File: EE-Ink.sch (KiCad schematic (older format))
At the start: 3 parts

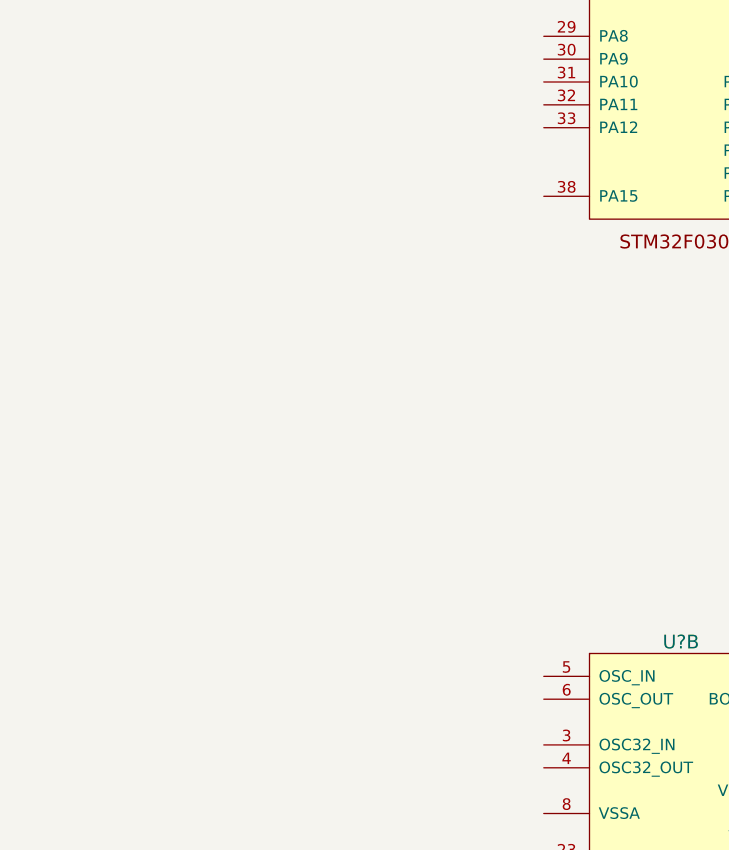
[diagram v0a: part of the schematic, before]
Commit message: Created drawing for the E-ink display and plopped it onto the schematic.
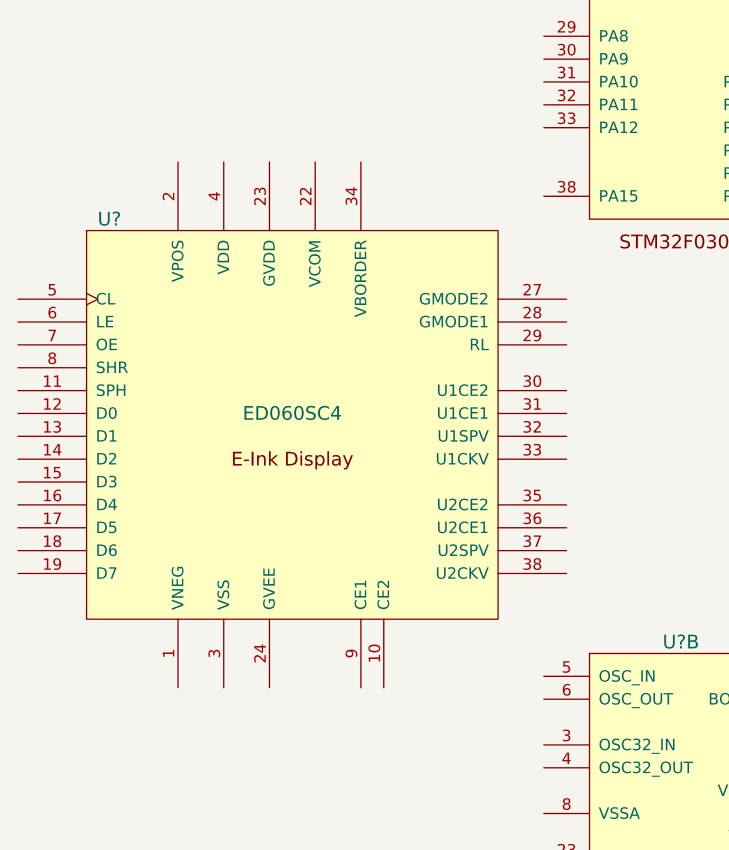
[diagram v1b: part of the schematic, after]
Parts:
- added U?: ED060SC4, symbol ED060SC4
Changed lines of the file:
@@
 LIBS:valves
 LIBS:stm32
+LIBS:e-ink
+LIBS:EE-Ink-cache
 EELAYER 25 0
 EELAYER END
@@
 	1    0    0    -1
 $EndComp
+$Comp
+L ED060SC4 U?
+U 1 1 58D7DC1F
+P 2250 4250
+F 0 "U?" H 1450 5150 60  0000 C CNN
+F 1 "ED060SC4" H 2250 4300 60  0000 C CNN
+F 2 "" H 2250 4250 60  0000 C CNN
+F 3 "" H 2250 4250 60  0000 C CNN
+	1    2250 4250
+	1    0    0    -1
+$EndComp

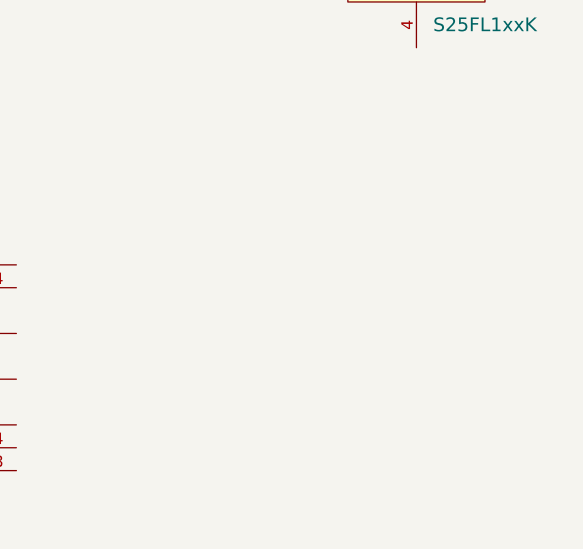
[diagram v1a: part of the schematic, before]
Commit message: Added dc to dc converter component.
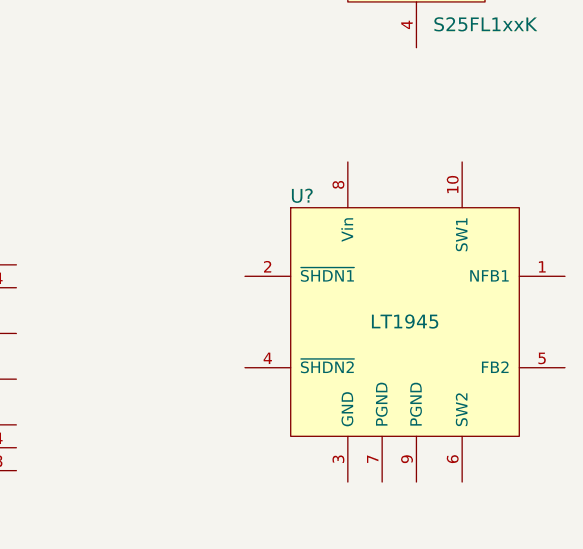
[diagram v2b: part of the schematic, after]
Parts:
- added U?: LT1945, symbol LT1945
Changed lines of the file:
@@
+	1    0    0    -1
+$EndComp
+$Comp
+L LT1945 U?
+U 1 1 58D7E9C0
+P 6250 5600
+F 0 "U?" H 5800 6150 60  0000 C CNN
+F 1 "LT1945" H 6250 5600 60  0000 C CNN
+F 2 "" H 6250 5600 60  0001 C CNN
+F 3 "" H 6250 5600 60  0001 C CNN
+	1    6250 5600
 	1    0    0    -1
 $EndComp

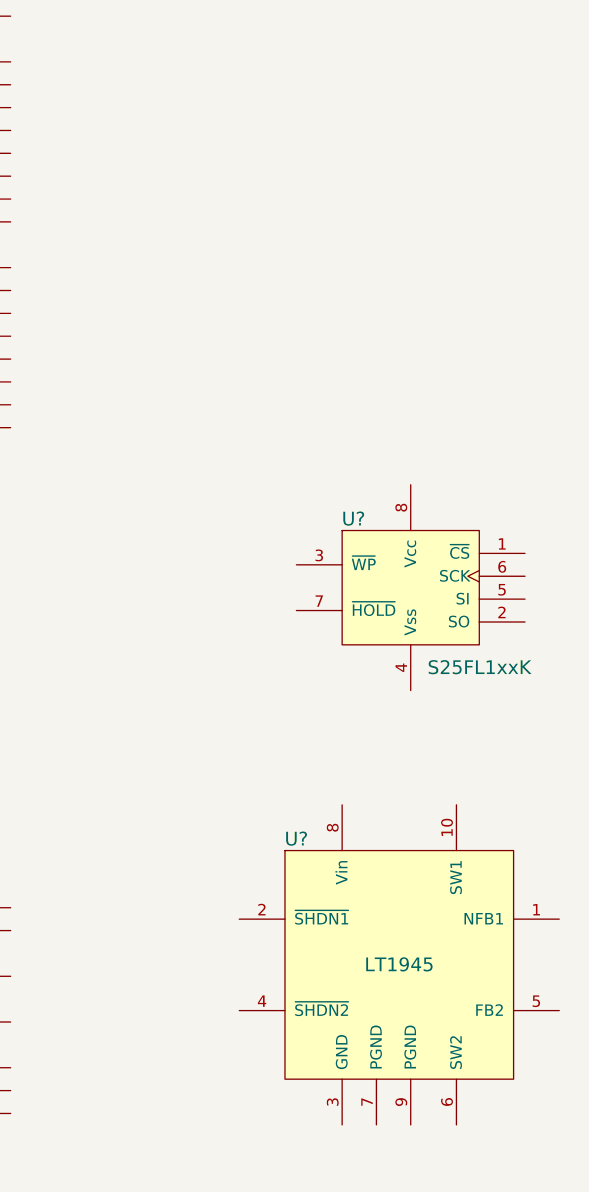
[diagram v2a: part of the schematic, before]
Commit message: Added battery charger component.
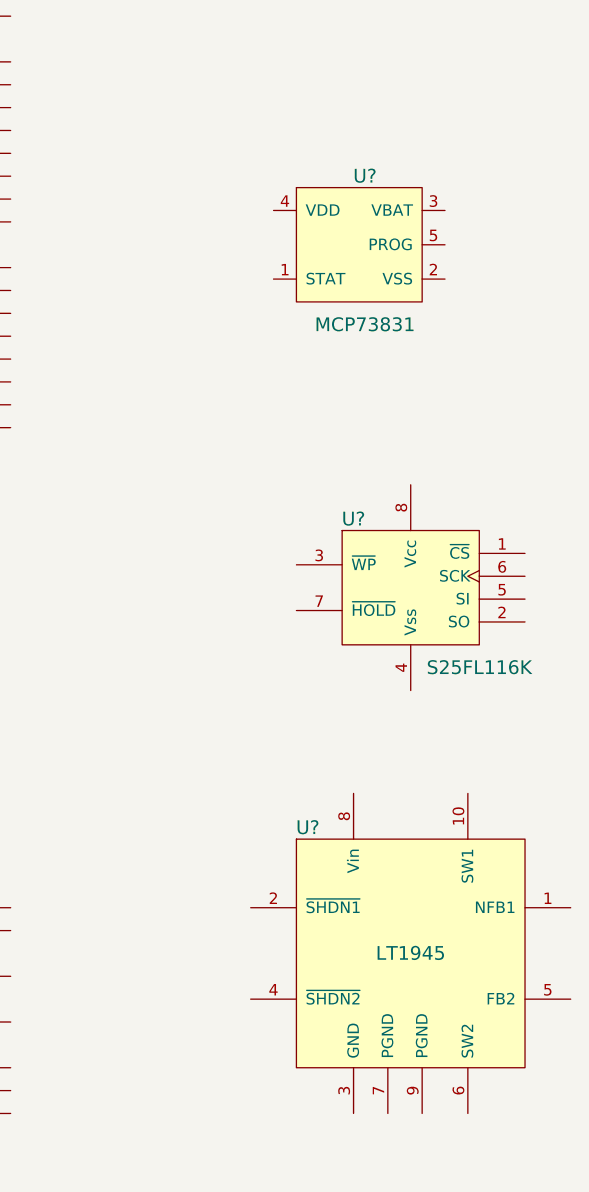
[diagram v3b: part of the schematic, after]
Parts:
- added U?: MCP73831, TO_SOT_Packages_SMD:SOT-23-5, symbol MCP73831
- U?: value S25FL1xxK -> S25FL116K
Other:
- moved on the sheet: U?
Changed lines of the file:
@@
 LIBS:stm32
 LIBS:e-ink
+LIBS:battery
 LIBS:EE-Ink-cache
 EELAYER 25 0
@@
 P 6300 3950
 F 0 "U?" H 6050 4250 60  0000 C CNN
-F 1 "S25FL1xxK" H 6600 3600 60  0000 C CNN
+F 1 "S25FL116K" H 6600 3600 60  0000 C CNN
 F 2 "" H 6200 4000 60  0001 C CNN
 F 3 "" H 6200 4000 60  0001 C CNN
@@
 L LT1945 U?
 U 1 1 58D7E9C0
-P 6250 5600
-F 0 "U?" H 5800 6150 60  0000 C CNN
-F 1 "LT1945" H 6250 5600 60  0000 C CNN
-F 2 "" H 6250 5600 60  0001 C CNN
-F 3 "" H 6250 5600 60  0001 C CNN
-	1    6250 5600
+P 6300 5550
+F 0 "U?" H 5850 6100 60  0000 C CNN
+F 1 "LT1945" H 6300 5550 60  0000 C CNN
+F 2 "" H 6300 5550 60  0001 C CNN
+F 3 "" H 6300 5550 60  0001 C CNN
+	1    6300 5550
 	1    0    0    -1
 $EndComp
+$Comp
+L MCP73831 U?
+U 1 1 58D81AF5
+P 6100 2450
+F 0 "U?" H 6100 2750 60  0000 C CNN
+F 1 "MCP73831" H 6100 2100 60  0000 C CNN
+F 2 "TO_SOT_Packages_SMD:SOT-23-5" H 6100 1900 60  0001 C CNN
+F 3 "https://www.adafruit.com/datasheets/MCP73831.pdf" H 6100 2000 60  0001 C CNN
+	1    6100 2450
+	1    0    0    -1
+$EndComp

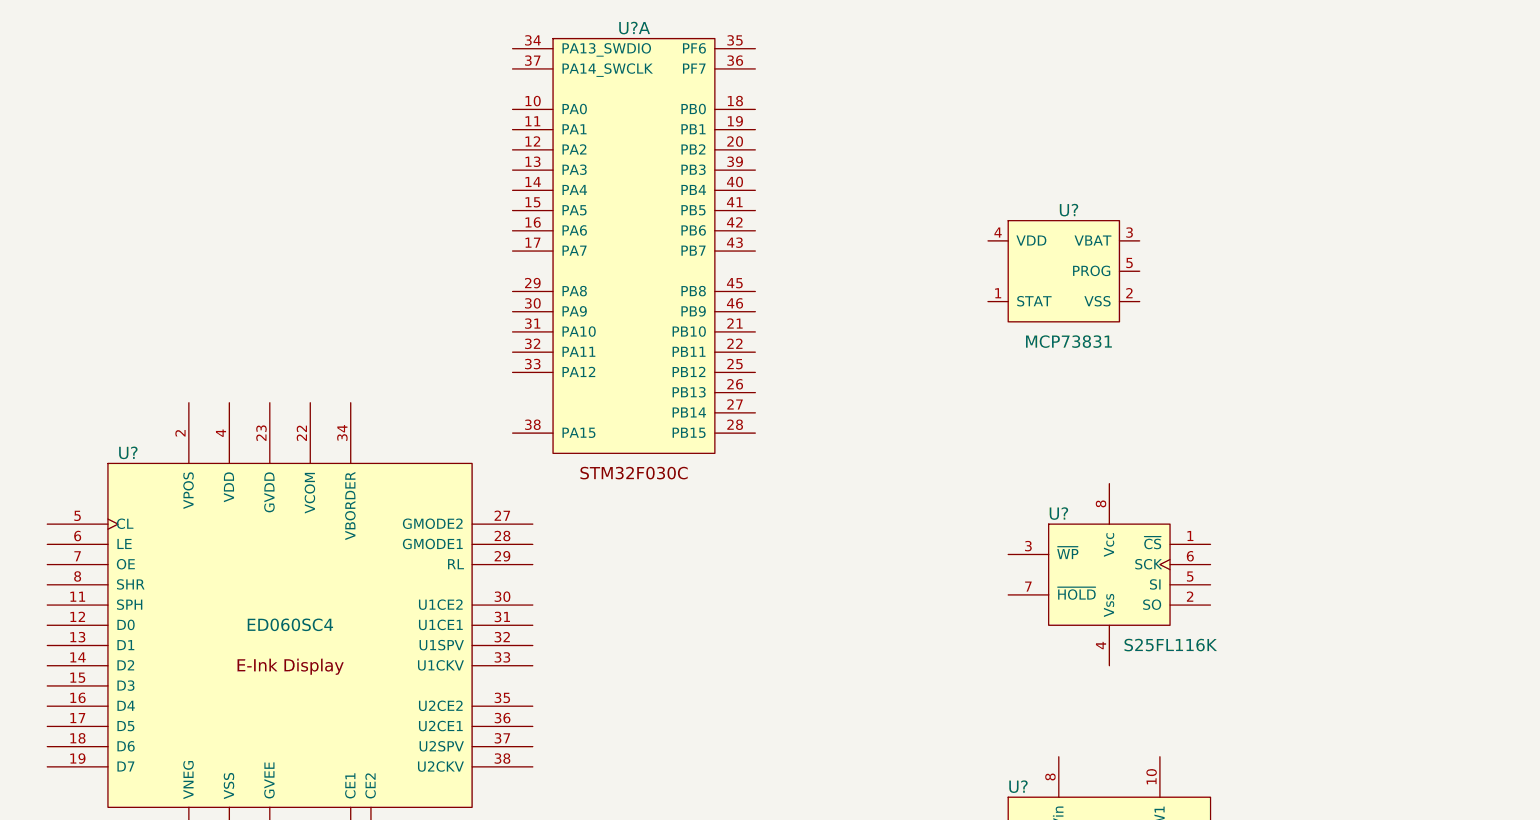
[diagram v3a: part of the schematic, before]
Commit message: Added several components.
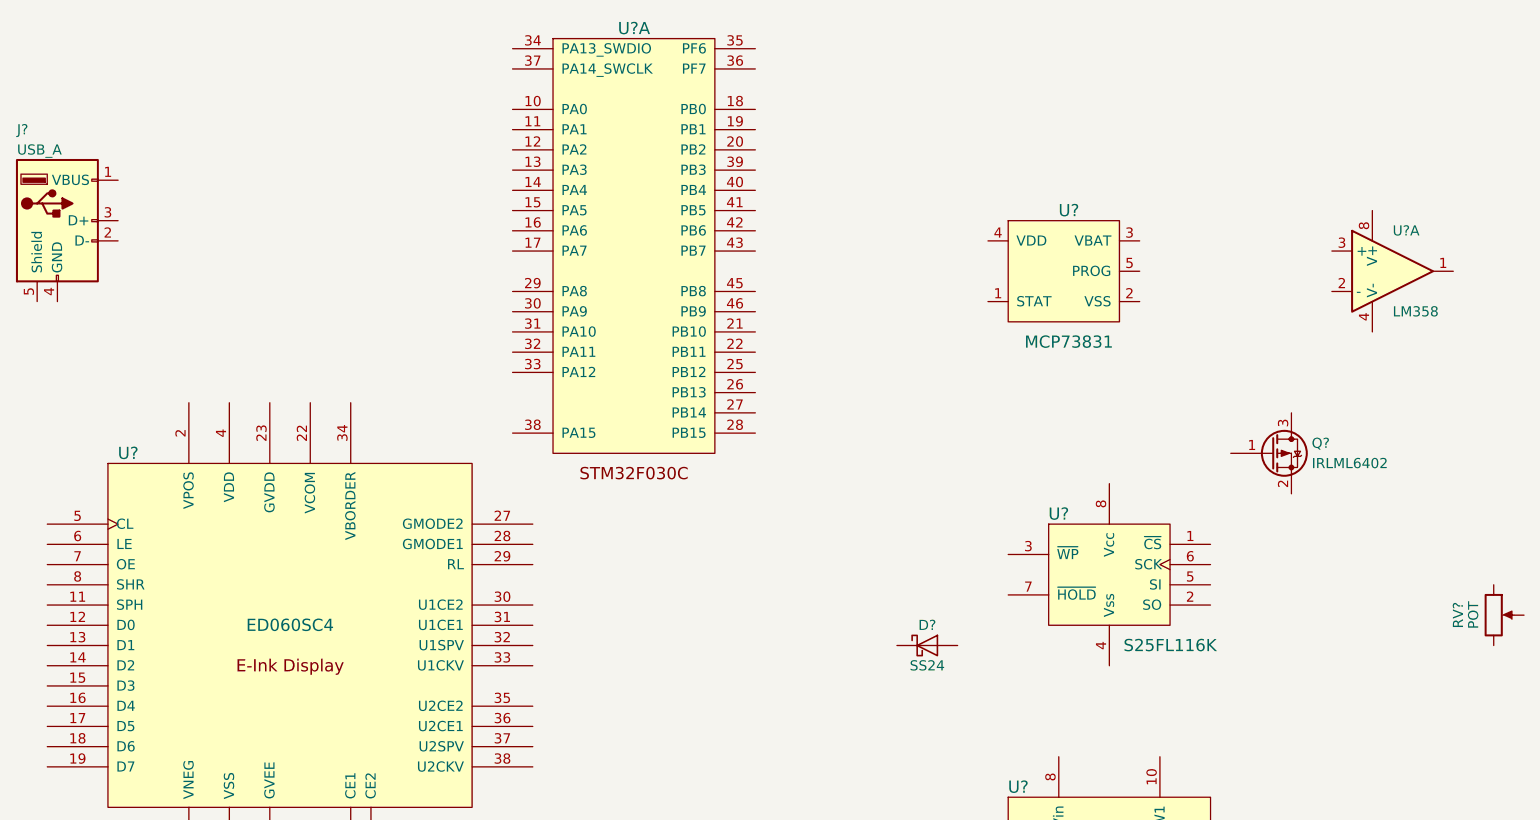
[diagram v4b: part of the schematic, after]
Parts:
- added D?: SS24, symbol D_Schottky
- added J?: USB_A, symbol USB_A
- added Q?: IRLML6402, symbol Q_PMOS_GSD
- added RV?: POT, symbol POT
- added U?: LM358, symbol LM358
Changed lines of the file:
@@
+	1    0    0    -1
+$EndComp
+$Comp
+L LM358 U?
+U 1 1 58D822C9
+P 7700 2450
+F 0 "U?" H 7700 2650 50  0000 L CNN
+F 1 "LM358" H 7700 2250 50  0000 L CNN
+F 2 "" H 7700 2450 50  0001 C CNN
+F 3 "" H 7700 2450 50  0001 C CNN
+	1    7700 2450
+	1    0    0    -1
+$EndComp
+$Comp
+L Q_PMOS_GSD Q?
+U 1 1 58D82351
+P 7100 3350
+F 0 "Q?" H 7300 3400 50  0000 L CNN
+F 1 "IRLML6402" H 7300 3300 50  0000 L CNN
+F 2 "" H 7300 3450 50  0001 C CNN
+F 3 "" H 7100 3350 50  0001 C CNN
+	1    7100 3350
+	1    0    0    -1
+$EndComp
+$Comp
+L D_Schottky D?
+U 1 1 58D829F1
+P 5400 4300
+F 0 "D?" H 5400 4400 50  0000 C CNN
+F 1 "SS24" H 5400 4200 50  0000 C CNN
+F 2 "" H 5400 4300 50  0001 C CNN
+F 3 "" H 5400 4300 50  0001 C CNN
+	1    5400 4300
+	1    0    0    -1
+$EndComp
+$Comp
+L USB_A J?
+U 1 1 58D82B24
+P 1100 2200
+F 0 "J?" H 900 2650 50  0000 L CNN
+F 1 "USB_A" H 900 2550 50  0000 L CNN
+F 2 "" H 1250 2150 50  0001 C CNN
+F 3 "" H 1250 2150 50  0001 C CNN
+	1    1100 2200
+	1    0    0    -1
+$EndComp
+$Comp
+L POT RV?
+U 1 1 58D82C23
+P 8200 4150
+F 0 "RV?" V 8025 4150 50  0000 C CNN
+F 1 "POT" V 8100 4150 50  0000 C CNN
+F 2 "" H 8200 4150 50  0001 C CNN
+F 3 "" H 8200 4150 50  0001 C CNN
+	1    8200 4150
 	1    0    0    -1
 $EndComp

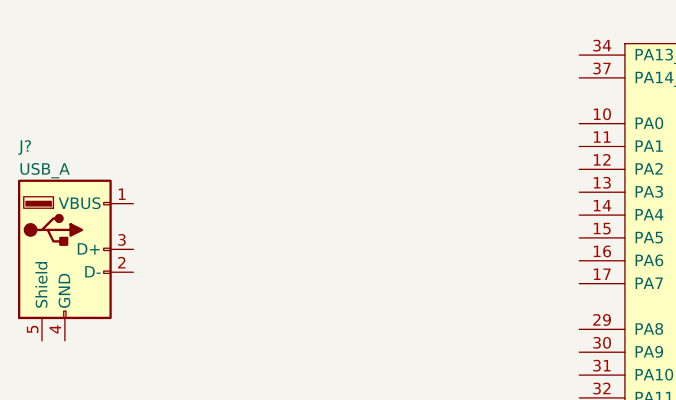
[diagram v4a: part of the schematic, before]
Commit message: Added regulator component.
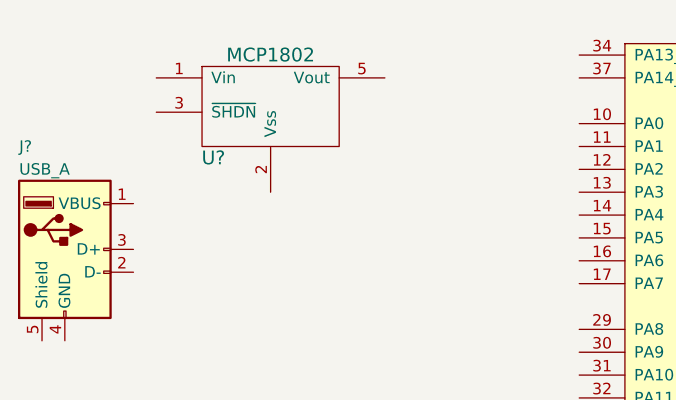
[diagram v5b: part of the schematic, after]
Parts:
- added U?: MCP1802, symbol MCP1802
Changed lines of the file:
@@
+	1    0    0    -1
+$EndComp
+$Comp
+L MCP1802 U?
+U 1 1 58D83813
+P 2000 1550
+F 0 "U?" H 1750 1300 60  0000 C CNN
+F 1 "MCP1802" H 2000 1750 60  0000 C CNN
+F 2 "" H 2000 1850 60  0001 C CNN
+F 3 "" H 2000 1850 60  0001 C CNN
+	1    2000 1550
 	1    0    0    -1
 $EndComp
